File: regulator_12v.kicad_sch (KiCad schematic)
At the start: 0 parts

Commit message: added 12v circuit, no values yet
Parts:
- added C19, C20: 0.1uF, symbol Device:C
- added C21, C22, C23, C24, C25, C26, C27, C28, C29: C, symbol Device:C
- added L1: 2.2uH, symbol Device:L
- added R7, R8, R9: R, symbol Device:R
- added U4: MAX25240AFFD/VY+, 21-100399_90-100137_ADI, symbol MAX25240:MAX25240AFFD_VY+
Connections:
- new net: C22.1, R7.2
- new net 12V_BST1: C20.1, U4.1 (BST1)
- new net 12V_BST2: C19.2, U4.14 (BST2)
- new net 12V_COMP: C21.1, R7.1, U4.17 (COMP)
- new net 12V_FB: R8.1, U4.16 (FB)
- new net 12V_LX1: C20.2, L1.1, U4.7 (LX1)
- new net 12V_LX2: C19.1, L1.2, U4.8 (LX2)
- new net 12V_VCC: C23.1, U4.21 (VCC)
- new net EN: U4.15 (EN)
- new net GND: C21.2, C22.2, C23.2, C24.2, C25.2, C26.2, C27.2, C28.2, C29.2, R9.2, U4.10 (PGND2), U4.22 (AGND), U4.5 (PGND1), U4.6 (PGND1), U4.9 (PGND2)
- new net OUT: C24.1, C25.1, C26.1, C27.1, R8.2, R9.1, U4.12 (OUT), U4.13 (OUT)
- new net PGOOD: U4.20 (PGOOD)
- new net SPS: U4.18 (SPS)
- new net SUP: C28.1, C29.1, U4.2 (SUP), U4.3 (SUP)
- new net SYNC: U4.19 (SYNC)

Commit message: added values
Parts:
- added C30: 22uF, symbol Device:C
- added C31: 47uF, symbol Device:C
- C21: value C -> 10pF
- C22: value C -> 2.7nF
- C23: value C -> 4.7uF
- C24, C25, C26, C27: value C -> 22uF
- C28, C29: value C -> 10uF
- R7: value R -> 51K
- R8: value R -> 140k
- R9: value R -> 10k
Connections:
- net GND: now also C30.2, C31.2
- net OUT: now also C30.1, C31.1

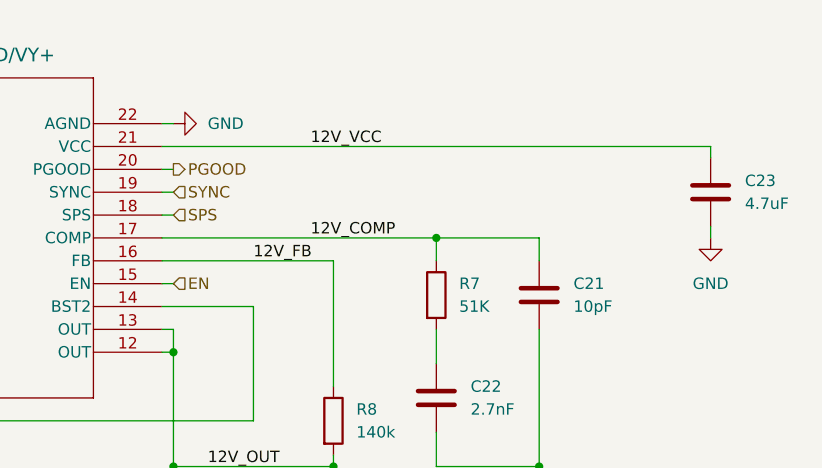
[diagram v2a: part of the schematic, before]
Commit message: connected sync and sps to vcc
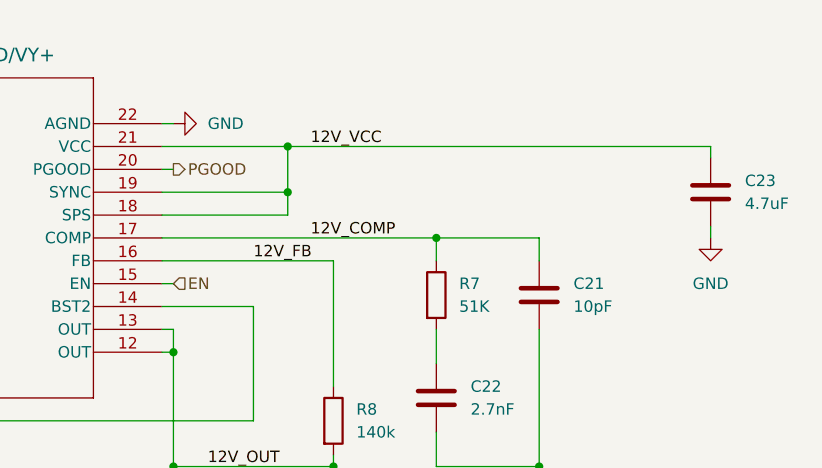
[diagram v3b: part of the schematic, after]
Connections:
- net SPS is gone; now on net 12V_VCC: U4.18 (SPS)
- net SYNC is gone; now on net 12V_VCC: U4.19 (SYNC)
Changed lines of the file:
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@@
+	)
+	(junction
+		(at 170.18 82.55)
+		(diameter 0)
+		(color 0 0 0 0)
 	)
 	(junction
@@
 	)
 	(junction
+		(at 170.18 87.63)
+		(diameter 0)
+		(color 0 0 0 0)
+	)
+	(junction
 		(at 110.49 133.35)
 		(diameter 0)
@@
 	(wire
 		(pts
-			(xy 156.21 87.63) (xy 157.48 87.63)
+			(xy 156.21 87.63) (xy 170.18 87.63)
 		)
 		(stroke
@@
 	(wire
 		(pts
+			(xy 170.18 87.63) (xy 170.18 82.55)
+		)
+		(stroke
+			(width 0)
+			(type default)
+		)
+	)
+	(wire
+		(pts
 			(xy 96.52 82.55) (xy 97.79 82.55)
 		)
@@
 	(wire
 		(pts
+			(xy 170.18 90.17) (xy 170.18 87.63)
+		)
+		(stroke
+			(width 0)
+			(type default)
+		)
+	)
+	(wire
+		(pts
 			(xy 186.69 92.71) (xy 186.69 95.25)
 		)
@@
 	(wire
 		(pts
-			(xy 156.21 90.17) (xy 157.48 90.17)
+			(xy 170.18 82.55) (xy 156.21 82.55)
+		)
+		(stroke
+			(width 0)
+			(type default)
+		)
+	)
+	(wire
+		(pts
+			(xy 156.21 90.17) (xy 170.18 90.17)
 		)
 		(stroke
@@
 	(wire
 		(pts
-			(xy 217.17 82.55) (xy 156.21 82.55)
+			(xy 217.17 82.55) (xy 170.18 82.55)
 		)
 		(stroke
@@
 		)
 	)
-	(hierarchical_label "SYNC"
-		(shape input)
-		(at 157.48 87.63 0)
-		(effects
-			(font
-				(size 1.27 1.27)
-			)
-			(justify left)
-		)
-	)
-	(hierarchical_label "SPS"
-		(shape input)
-		(at 157.48 90.17 0)
-		(effects
-			(font
-				(size 1.27 1.27)
-			)
-			(justify left)
-		)
-	)

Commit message: bms nearly finished
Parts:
- R7: value 51K -> 51k
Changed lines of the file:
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@@
 			)
 		)
-		(property "Value" "51K"
+		(property "Value" "51k"
 			(at 189.23 100.3299 0)
 			(effects

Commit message: added footprints to all components in 12v regulator
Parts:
- C19, C20, C22: footprint (none) -> Capacitor_SMD:C_0603_1608Metric
- C21: footprint (none) -> Capacitor_SMD:C_0402_1005Metric
- C23, C24, C25, C26, C27, C30, C31: footprint (none) -> Capacitor_SMD:C_1206_3216Metric
- C28, C29: footprint (none) -> Capacitor_SMD:C_0805_2012Metric
- L1: footprint (none) -> Inductor_SMD:L_Coilcraft_XAL7070-XXX
- R7, R8: footprint (none) -> Resistor_SMD:R_0402_1005Metric
- R9: footprint (none) -> Resistor_SMD:R_0603_1608Metric
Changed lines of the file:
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@@
 			)
 		)
-		(property "Footprint" ""
+		(property "Footprint" "Capacitor_SMD:C_1206_3216Metric"
 			(at 111.4552 132.08 0)
 			(effects
@@
 			)
 		)
-		(property "Footprint" ""
+		(property "Footprint" "Capacitor_SMD:C_0603_1608Metric"
 			(at 87.3252 90.17 0)
 			(effects
@@
 			)
 		)
-		(property "Footprint" ""
+		(property "Footprint" "Capacitor_SMD:C_1206_3216Metric"
 			(at 147.0152 132.08 0)
 			(effects
@@
 			)
 		)
-		(property "Footprint" ""
+		(property "Footprint" "Capacitor_SMD:C_1206_3216Metric"
 			(at 98.7552 132.08 0)
 			(effects
@@
 			)
 		)
-		(property "Footprint" ""
+		(property "Footprint" "Capacitor_SMD:C_1206_3216Metric"
 			(at 158.4452 132.08 0)
 			(effects
@@
 			)
 		)
-		(property "Footprint" ""
+		(property "Footprint" "Capacitor_SMD:C_1206_3216Metric"
 			(at 218.1352 91.44 0)
 			(effects
@@
 			)
 		)
-		(property "Footprint" ""
+		(property "Footprint" "Capacitor_SMD:C_1206_3216Metric"
 			(at 124.1552 132.08 0)
 			(effects
@@
 			)
 		)
-		(property "Footprint" ""
+		(property "Footprint" "Resistor_SMD:R_0402_1005Metric"
 			(at 184.912 99.06 90)
 			(effects
@@
 			)
 		)
-		(property "Footprint" ""
+		(property "Footprint" "Capacitor_SMD:C_0402_1005Metric"
 			(at 199.0852 102.87 0)
 			(effects
@@
 			)
 		)
-		(property "Footprint" ""
+		(property "Footprint" "Resistor_SMD:R_0603_1608Metric"
 			(at 173.482 123.19 90)
 			(effects
@@
 			)
 		)
-		(property "Footprint" ""
+		(property "Footprint" "Inductor_SMD:L_Coilcraft_XAL7070-XXX"
 			(at 86.36 96.52 0)
 			(effects
@@
 			)
 		)
-		(property "Footprint" ""
+		(property "Footprint" "Capacitor_SMD:C_1206_3216Metric"
 			(at 135.5852 132.08 0)
 			(effects
@@
 			)
 		)
-		(property "Footprint" ""
+		(property "Footprint" "Capacitor_SMD:C_0603_1608Metric"
 			(at 87.3252 110.49 0)
 			(effects
@@
 			)
 		)
-		(property "Footprint" ""
+		(property "Footprint" "Resistor_SMD:R_0402_1005Metric"
 			(at 173.482 113.03 90)
 			(effects
@@
 			)
 		)
-		(property "Footprint" ""
+		(property "Footprint" "Capacitor_SMD:C_0805_2012Metric"
 			(at 105.1052 90.17 0)
 			(effects
@@
 			)
 		)
-		(property "Footprint" ""
+		(property "Footprint" "Capacitor_SMD:C_0603_1608Metric"
 			(at 187.6552 114.3 0)
 			(effects
@@
 			)
 		)
-		(property "Footprint" ""
+		(property "Footprint" "Capacitor_SMD:C_0805_2012Metric"
 			(at 98.7552 90.17 0)
 			(effects

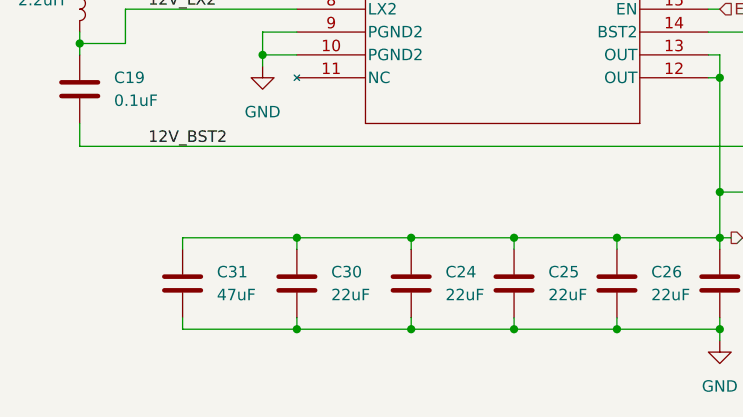
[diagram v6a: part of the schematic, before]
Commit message: probably didn't need that many capacitors on the 12v output
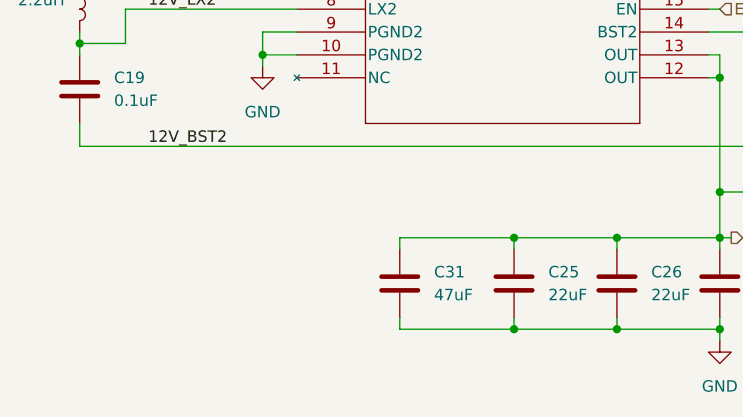
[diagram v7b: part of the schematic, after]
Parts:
- removed C24, C30: 22uF, Capacitor_SMD:C_1206_3216Metric, symbol Device:C
- U4: footprint 21-100399_90-100137_ADI -> International_Footprints:21-100399_90-100137_ADI
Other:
- moved on the sheet: C31
